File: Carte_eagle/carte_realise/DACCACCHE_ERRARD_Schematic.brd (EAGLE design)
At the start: 100 x 80 mm, 10 parts, among them CON1 CON-1X2-SPOX-M-2.50, CON2 CON-1X2-SPOX-M-2.50, U1 DOGM163

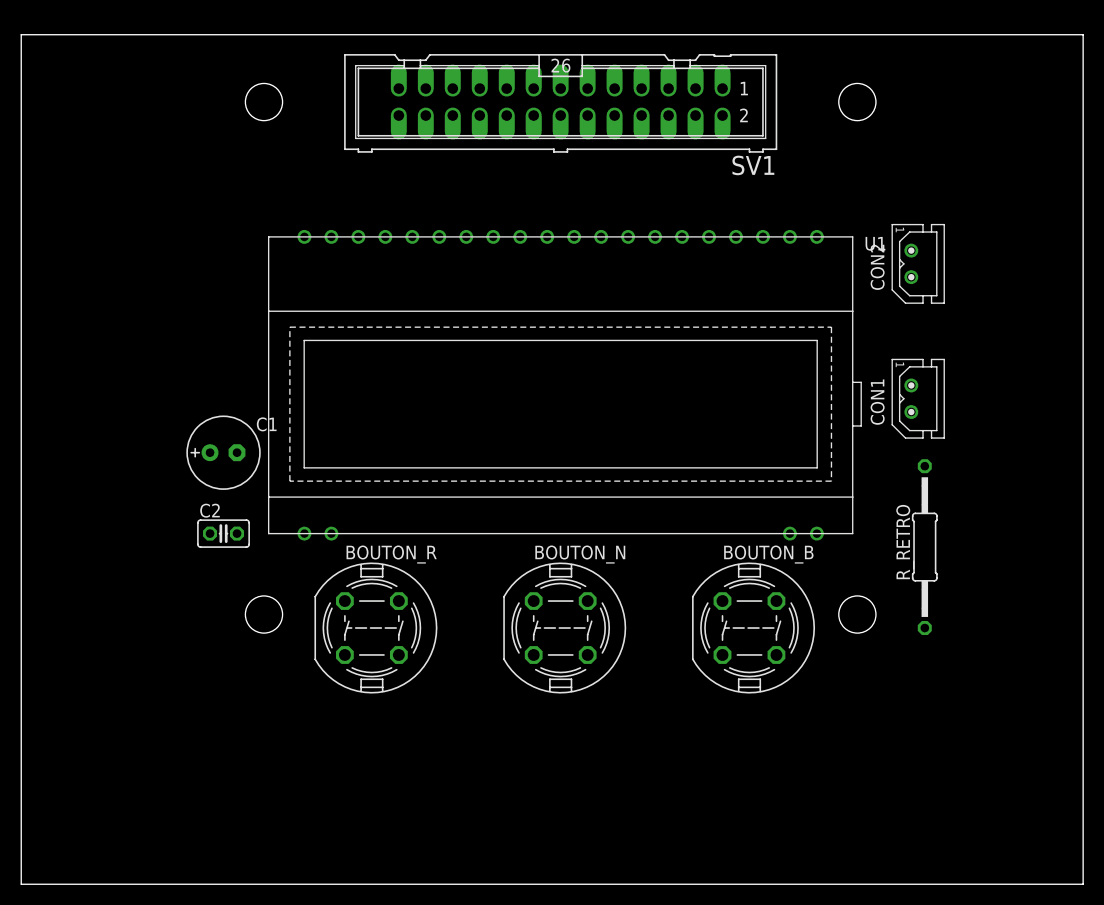
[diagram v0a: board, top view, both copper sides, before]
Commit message: update board et schematics
finalisation du schema avec le changement des pins de l'ecran et des boutons
finalisation de la carte avec l'epaisseur des cables et le cassage des angles droits
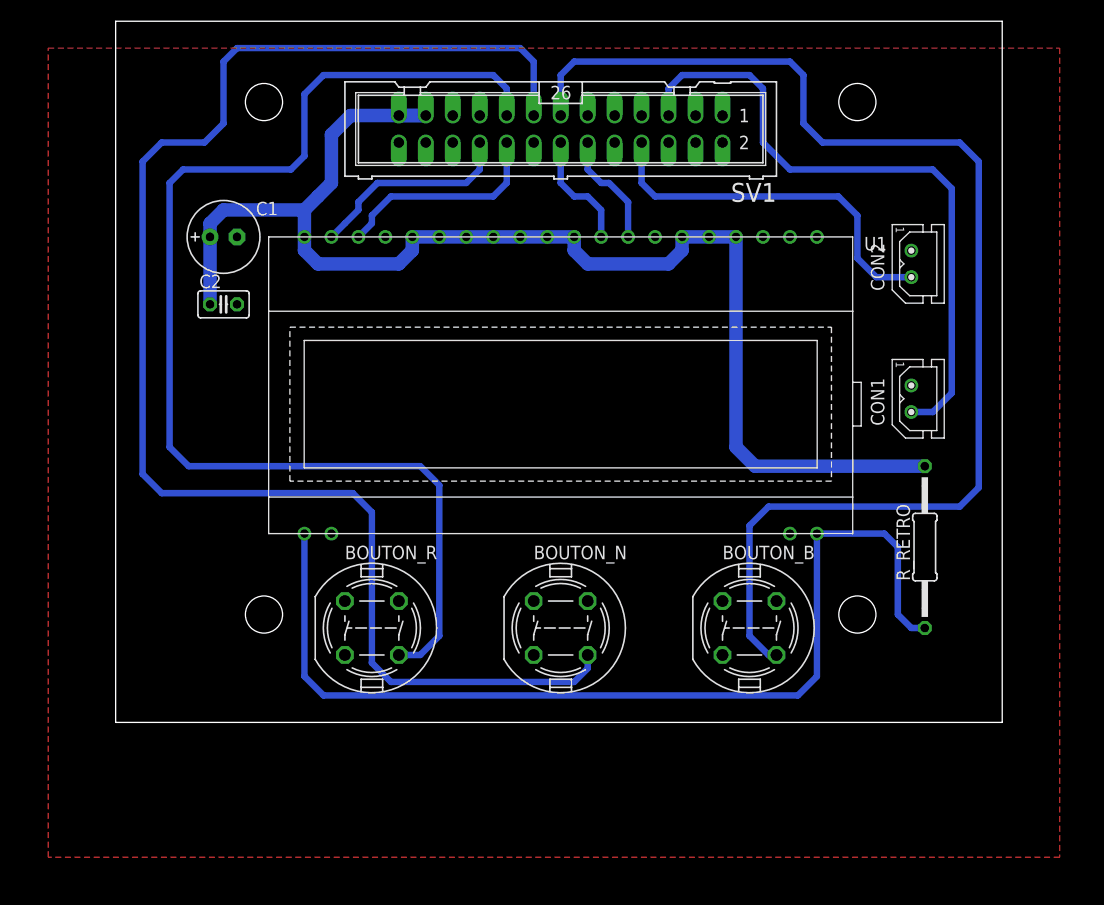
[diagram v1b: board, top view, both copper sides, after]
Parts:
- moved C2 21.6 mm to (19.1, 54.6)
- moved C1 20.3 mm to (19.1, 61.0)
- moved SV1 2.54 mm to (50.8, 71.1)
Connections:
- net N$1 renamed RHETRO_RES
- removed net RB0_RS: SV1.17, U1.39
- removed net RB1_!CSB: SV1.15, U1.38
- removed net RB3_CLK: SV1.11, U1.29
- removed net RB4_SDO: SV1.9, U1.28
- removed net RE0_BOUT_B: BOUTON_B.3, SV1.20
- removed net RE1_BOUT_N: BOUTON_N.3, SV1.18
- removed net RE2_BOUT_R: BOUTON_R.3, SV1.16
- new net RB0_BOUT_R: BOUTON_R.3, SV1.17
- new net RB1_BOUT_N: BOUTON_N.3, SV1.15
- new net RB2_BOUT_B: BOUTON_B.3, SV1.13
- new net RE0_RS: SV1.20, U1.39
- new net RE1_!CSB: SV1.18, U1.38
- new net RE3_CLK: SV1.14, U1.29
- new net RE4_SDO: SV1.12, U1.28
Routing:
- net RB1_BOUT_N: track 0.00 -> 139.8 mm
- net +5V: track 0.00 -> 126.0 mm
- net RB2_BOUT_B: track 0.00 -> 117.7 mm
- net RB0_BOUT_R: track 0.00 -> 112.9 mm
- net RHETRO_RES: track 0.00 -> 94.2 mm
- net RC13_U1ATX: track 0.00 -> 60.9 mm
- net RC14_U1ARX: track 0.00 -> 35.2 mm
- net RE1_!CSB: track 0.00 -> 20.3 mm
- net RE0_RS: track 0.00 -> 19.6 mm
- net RE3_CLK: track 0.00 -> 11.2 mm
- net RE4_SDO: track 0.00 -> 10.9 mm
- added copper zone on layer 1, net GND
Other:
- board size 100 x 80 mm -> 83.5 x 66 mm
